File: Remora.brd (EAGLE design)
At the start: 86.4 x 66.7 mm, 81 parts, among them IC1 MCP23017, J2 GROVE-I2C, P1 PADSMALL, T1 2N3904, T2 BSS138

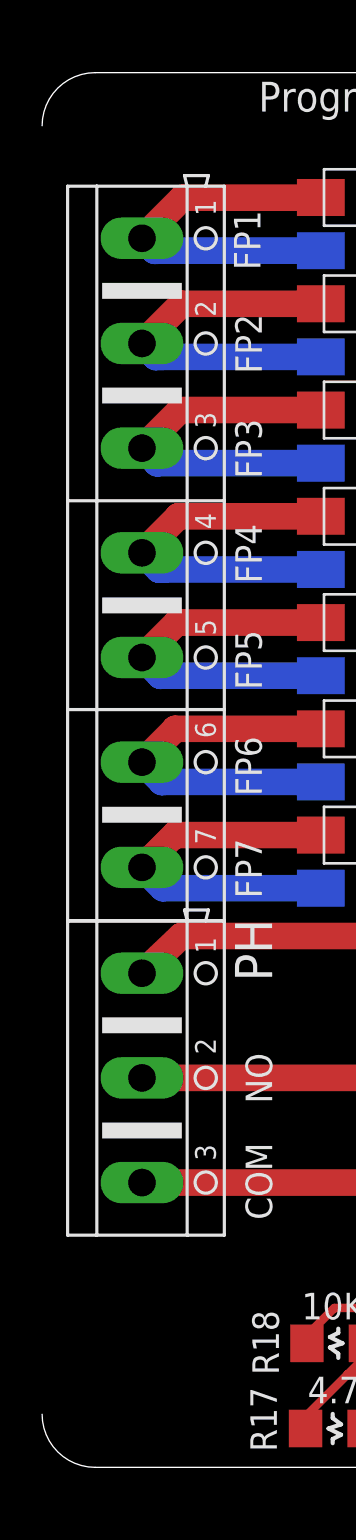
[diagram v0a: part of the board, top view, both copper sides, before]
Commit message: Correction d'une erreur dans la couche dimension
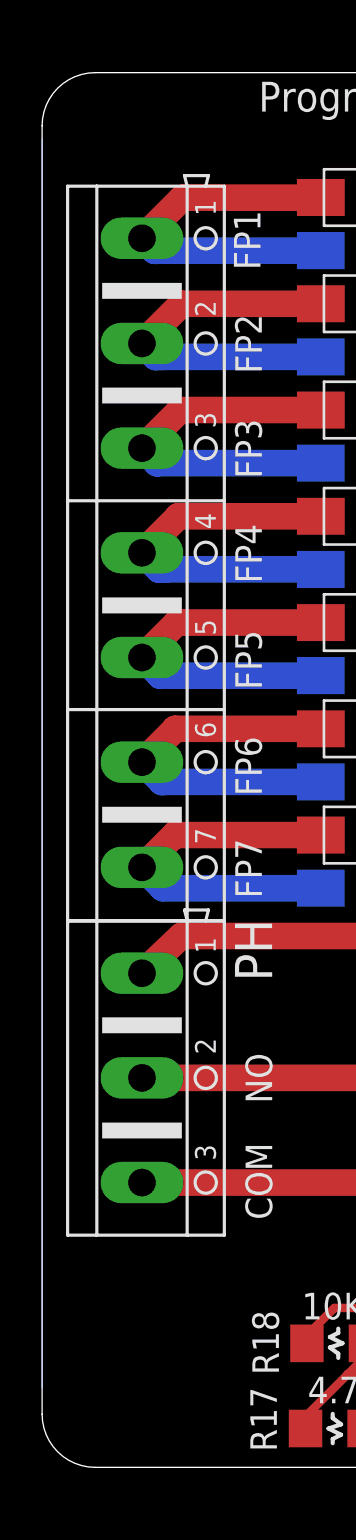
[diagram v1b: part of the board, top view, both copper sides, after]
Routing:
- net N$20: track 0.00 -> 59.7 mm
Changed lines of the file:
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@@
 <wire x1="2.54" y1="0" x2="0" y2="2.54" width="0.0254" layer="20" curve="-90"/>
 <dimension x1="0" y1="71.755" x2="86.36" y2="71.755" x3="43.18" y3="-6.985" textsize="1.778" layer="47"/>
-<dimension x1="-6.35" y1="66.675" x2="-6.35" y2="0" x3="-11.43" y3="33.3375" textsize="1.778" layer="47"/>
+<dimension x1="0" y1="66.675" x2="0" y2="0" x3="-5.08" y3="33.3375" textsize="1.778" layer="47"/>
 <text x="73.369" y="56.418" size="1.27" layer="26" font="vector" ratio="15" rot="MR270">5V</text>
 <text x="76.4805" y="57.561" size="1.27" layer="26" font="vector" ratio="15" rot="MR270">3V3</text>
 <text x="10.9982" y="17.399" size="1.27" layer="25" font="vector" ratio="18" rot="R90">NO</text>
 <text x="10.9982" y="11.8364" size="1.27" layer="25" font="vector" ratio="18" rot="R90">COM</text>
+<wire x1="0" y1="64.135" x2="0" y2="2.54" width="0.0254" layer="20"/>
 </plain>
 <attributes>
@@
 <wire x1="25.0844" y1="13.6144" x2="26.837" y2="15.24" width="1.27" layer="1"/>
 </signal>
+<signal name="N$20">
+<wire x1="0" y1="3.81" x2="0" y2="63.5" width="0.0254" layer="16"/>
+</signal>
 </signals>
